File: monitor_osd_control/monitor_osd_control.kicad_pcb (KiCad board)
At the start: 2 copper layers, 50 x 58 mm, 21 parts, among them J1 Conn_01x09, J2 Conn_01x09, J3 Conn_01x05, J4 Conn_01x05, SW1 SW_Push, SW2 SW_Push, SW3 SW_Push, SW4 SW_Push, SW5 SW_Push, SW6 SW_Push, U1 TSSP58038

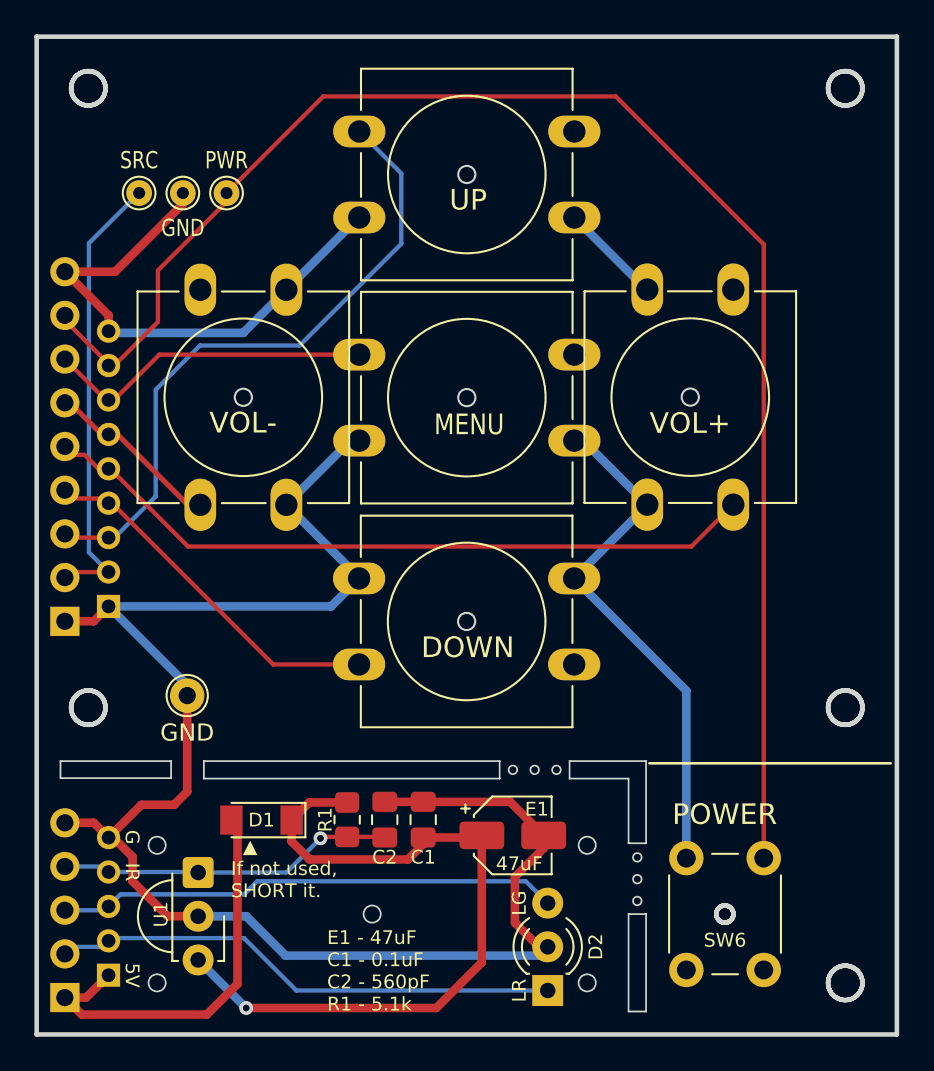
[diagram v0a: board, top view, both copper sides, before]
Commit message: 커넥터 위치 미세하게 안쪽으로 조정
Signed-off-by: Ju, Gyeong-min <jcmh74@gmail.com>
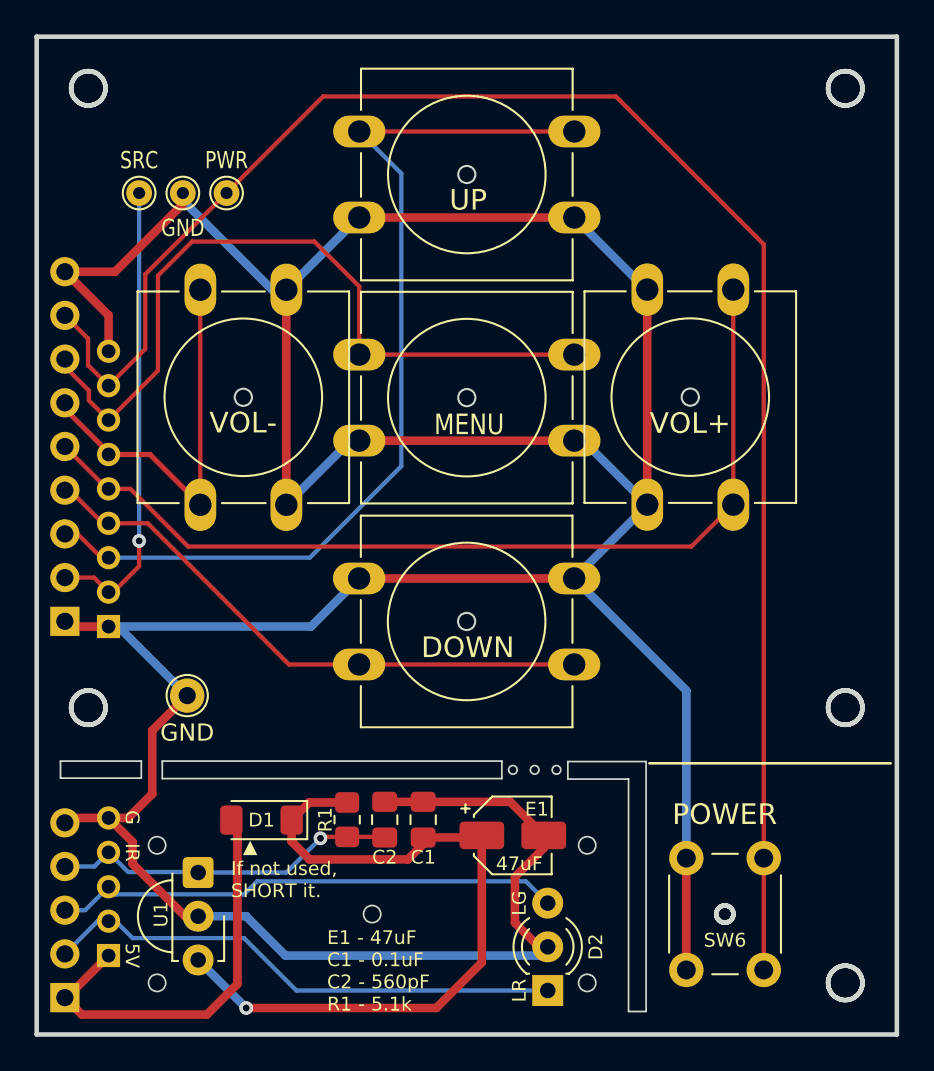
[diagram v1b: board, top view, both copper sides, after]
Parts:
- moved J1 1.17 mm to (132.8, 96.1)
- moved J3 1.14 mm to (132.8, 115.2)
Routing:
- net GND: track 166.7 -> 226.0 mm
- net /MENU: track 19.2 -> 44.2 mm
- net /UP: track 37.9 -> 55.3 mm
- net /VOL_M: track 10.3 -> 23.1 mm
- net /DOWN: track 21.3 -> 33.8 mm
- net /VOL_P: track 42.3 -> 54.8 mm
- net /POWER: track 89.8 -> 98.5 mm
- net /IRIN: track 19.3 -> 20.3 mm
- net /LED_R: track 29.7 -> 30.5 mm
- net /SOURCE: track 26.4 -> 27.0 mm, vias 0 -> 1
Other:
- outline, holes or cut-outs redrawn
- board text added: "Rev.5"
- board text removed: "Rev.4"

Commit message: 버튼을 12mm와 6mm 겸용으로
Signed-off-by: Ju, Gyeong-min <jcmh74@gmail.com>
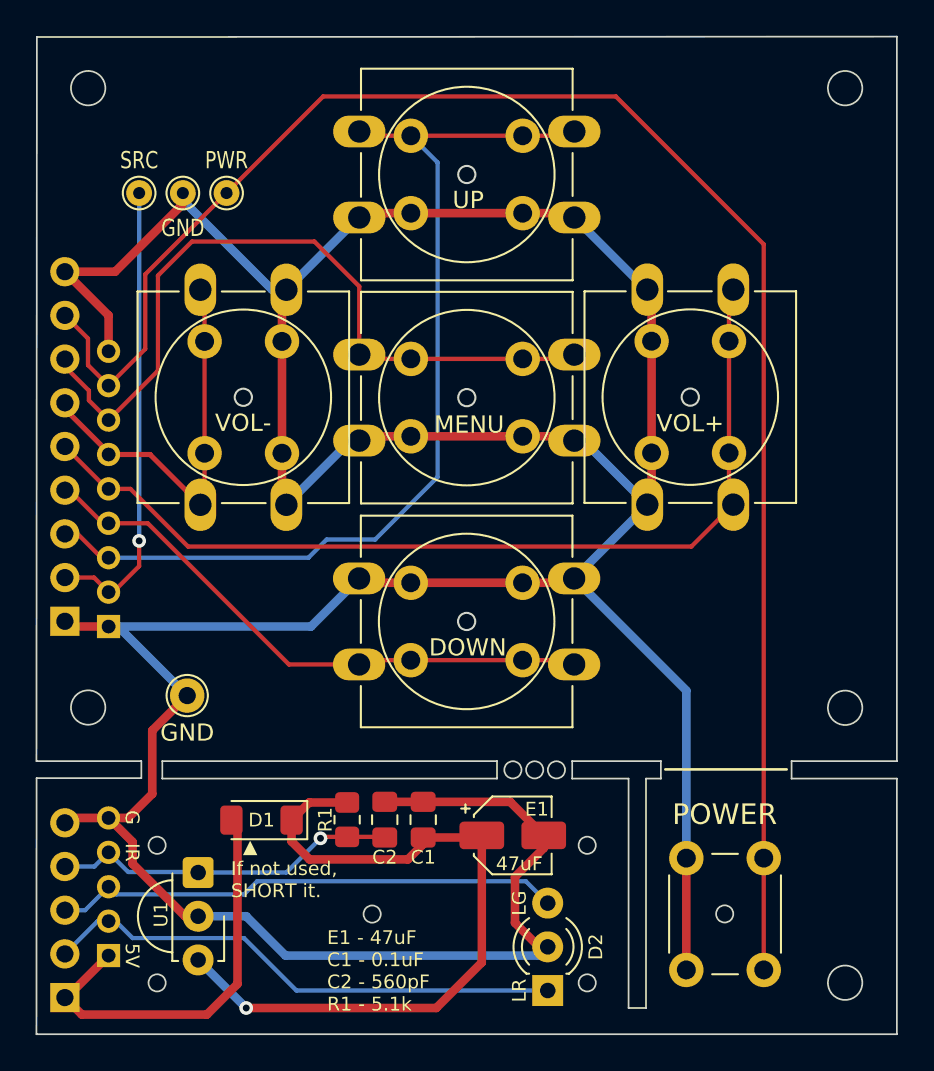
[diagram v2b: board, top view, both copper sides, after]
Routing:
- net /UP: track 55.3 -> 57.4 mm
- net GND: track 226.0 -> 227.0 mm
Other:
- outline, holes or cut-outs redrawn
